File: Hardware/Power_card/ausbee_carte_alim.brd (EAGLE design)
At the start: 64.8 x 71.4 mm, 17 parts

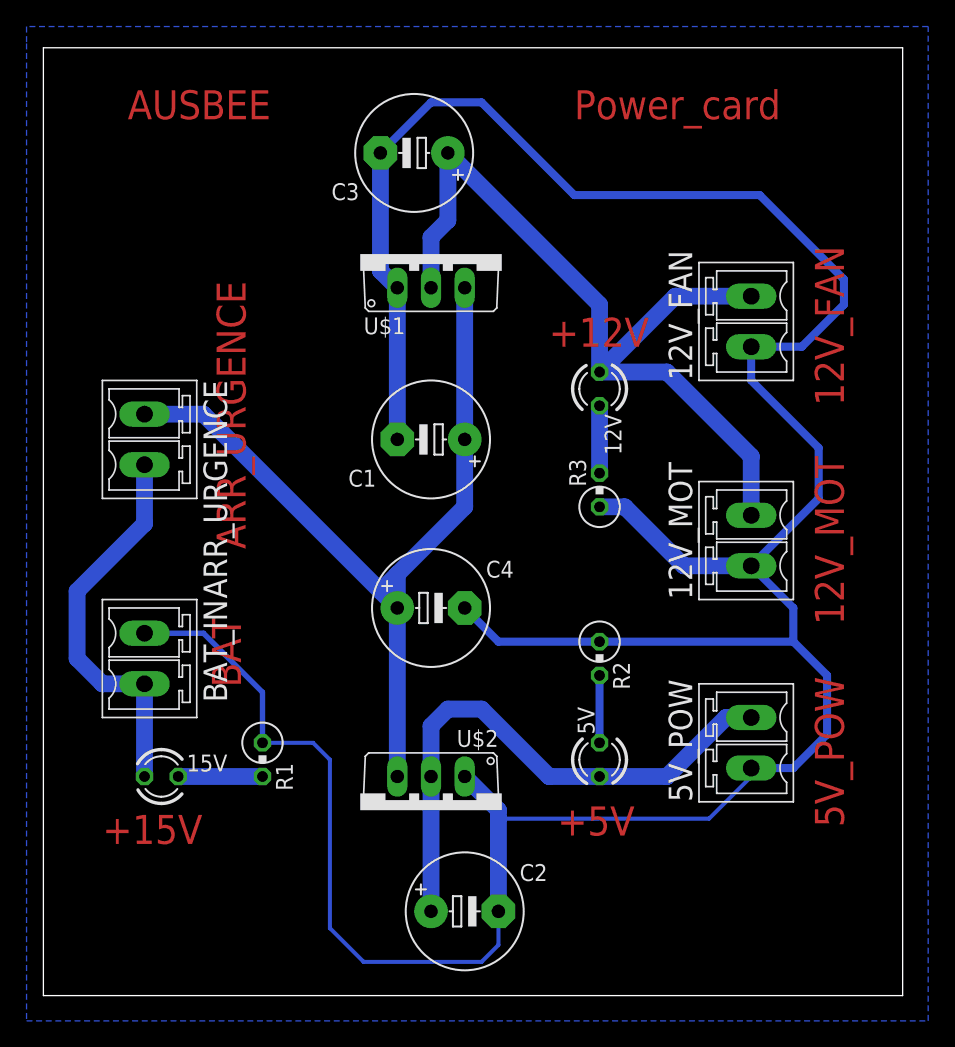
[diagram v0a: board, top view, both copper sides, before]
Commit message: add holes in board
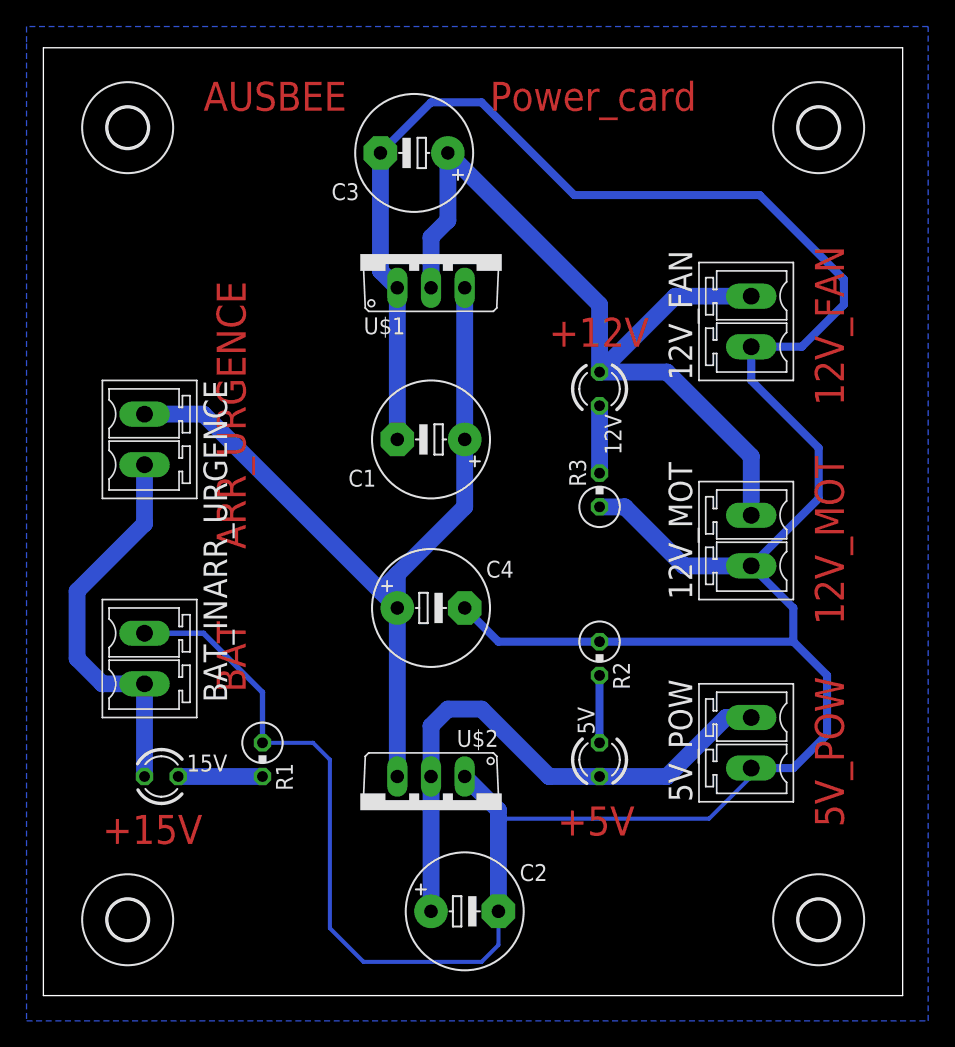
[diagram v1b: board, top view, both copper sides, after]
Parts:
- added H1, H2, H3, H4: MOUNT-HOLE3.0, holes:3,0
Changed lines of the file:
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@@
 <wire x1="64.75" y1="71.425" x2="0" y2="71.425" width="0" layer="20"/>
 <wire x1="0" y1="71.425" x2="0" y2="0" width="0" layer="20"/>
-<text x="12.7" y="28.575" size="2.1844" layer="1" font="vector" ratio="9" rot="R270">BAT</text>
+<text x="15.24" y="22.86" size="2.1844" layer="1" font="vector" ratio="9" rot="SR90">BAT</text>
 <text x="15.24" y="33.655" size="2.1844" layer="1" font="vector" ratio="10" rot="R90">ARR_URGENCE</text>
 <text x="60.325" y="12.7" size="2.1844" layer="1" font="vector" ratio="10" rot="R90">5V_POW</text>
 <text x="60.325" y="27.94" size="2.1844" layer="1" font="vector" ratio="10" rot="R90">12V_MOT</text>
 <text x="60.325" y="44.45" size="2.1844" layer="1" font="vector" ratio="10" rot="R90">12V_FAN</text>
-<text x="6.35" y="66.04" size="2.1844" layer="1" font="vector" ratio="10">AUSBEE</text>
-<text x="40.005" y="66.04" size="2.1844" layer="1" font="vector" ratio="10">Power_card</text>
+<text x="12.065" y="66.675" size="2.1844" layer="1" font="vector" ratio="10">AUSBEE</text>
+<text x="33.655" y="66.675" size="2.1844" layer="1" font="vector" ratio="10">Power_card</text>
 <text x="4.445" y="11.43" size="2.1844" layer="1" font="vector" ratio="10">+15V</text>
 <text x="38.735" y="12.065" size="2.1844" layer="1" font="vector" ratio="10">+5V</text>
@@
 <element name="12V_MOT" library="con-phoenix-381_l" package="MCV2" value="MCV2" x="53.34" y="34.29" rot="R90"/>
 <element name="12V_FAN" library="con-phoenix-381_l" package="MCV2" value="MCV2" x="53.34" y="50.8" rot="R90"/>
+<element name="H1" library="holes" package="3,0" value="MOUNT-HOLE3.0" x="6.35" y="5.715"/>
+<element name="H2" library="holes" package="3,0" value="MOUNT-HOLE3.0" x="58.42" y="5.715"/>
+<element name="H3" library="holes" package="3,0" value="MOUNT-HOLE3.0" x="58.42" y="65.405"/>
+<element name="H4" library="holes" package="3,0" value="MOUNT-HOLE3.0" x="6.35" y="65.405"/>
 </elements>
 <signals>
